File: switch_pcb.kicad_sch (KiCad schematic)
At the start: 6 parts, among them J1 Screw_Terminal_01x04, SW1 SW_Push_SPDT

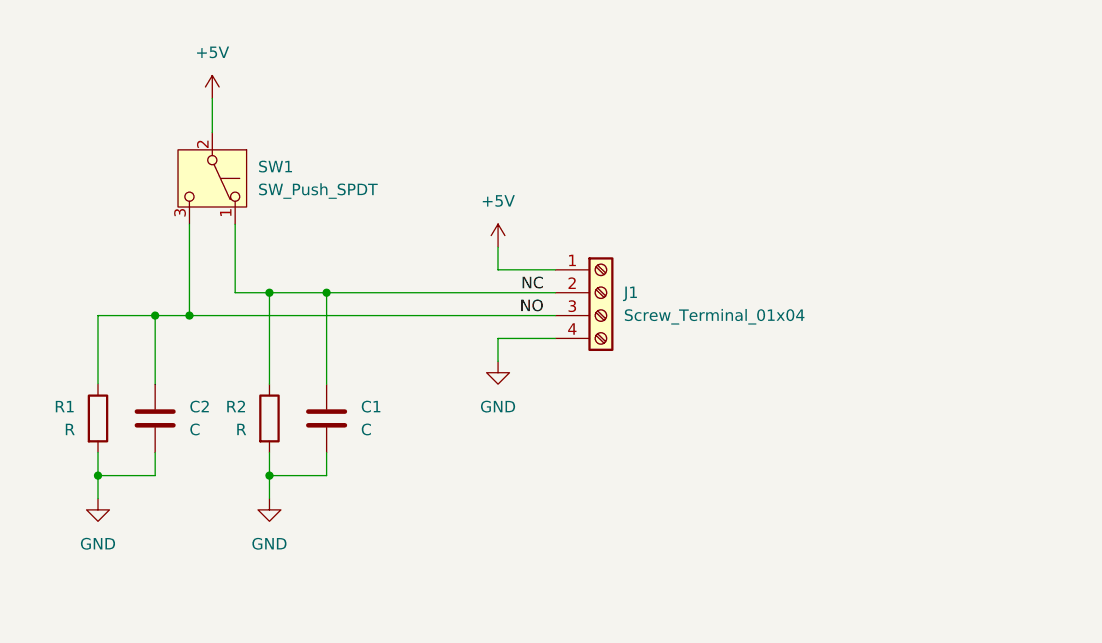
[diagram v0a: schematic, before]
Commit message: Add some footprints and mounting holes
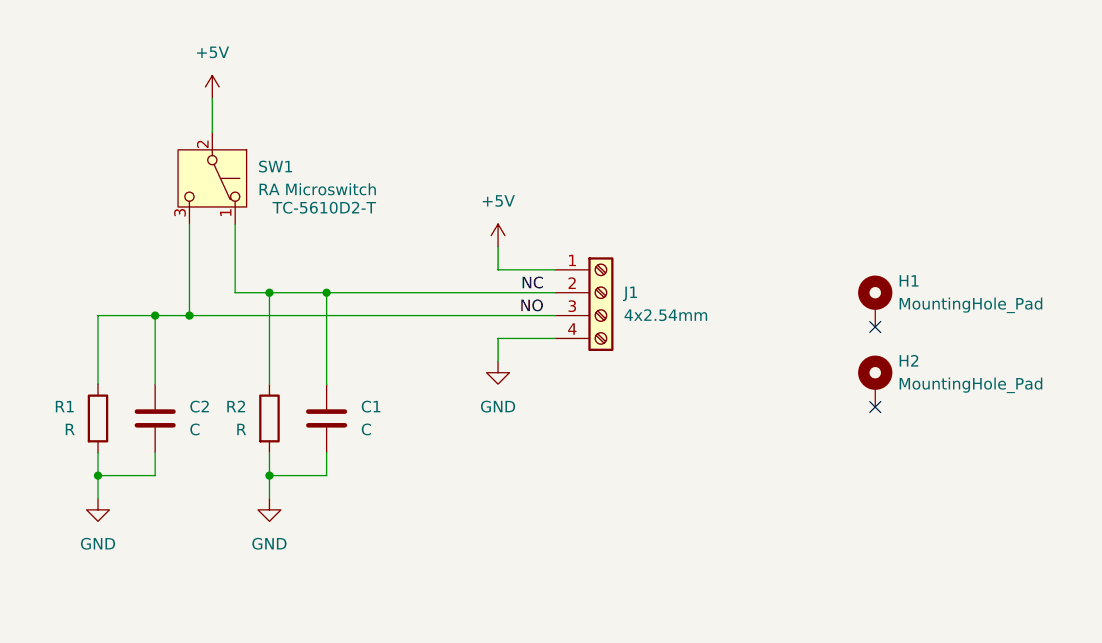
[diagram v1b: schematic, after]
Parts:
- added H1, H2: MountingHole_Pad, symbol Mechanical:MountingHole_Pad
- C1, C2: footprint (none) -> Capacitor_THT:C_Disc_D9.0mm_W5.0mm_P5.00mm
- J1: value Screw_Terminal_01x04 -> 4x2.54mm; footprint (none) -> TerminalBlock_Phoenix:TerminalBlock_Phoenix_MPT-0,5-4-2.54_1x04_P2.54mm_Horizontal; JLC (none) -> C5188444
- R1, R2: footprint (none) -> Resistor_THT:R_Axial_DIN0207_L6.3mm_D2.5mm_P10.16mm_Horizontal
- SW1: value SW_Push_SPDT -> RA Microswitch; JLC (none) -> C504864; MFR (none) -> TC-5610D2-T
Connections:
- no-connect marks 0 -> 2
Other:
- title: (none) -> 2020 Extrusion Microswitch Mount
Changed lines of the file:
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@@
 	(generator_version "8.0")
 	(paper "A4")
+	(title_block
+		(title "2020 Extrusion Microswitch Mount")
+		(comment 1 "All components are through-hole")
+	)
 	(junction
 		(at 127 81.28)
@@
 		(diameter 0)
 		(color 0 0 0 0)
+	)
+	(no_connect
+		(at 187.96 85.09)
+	)
+	(no_connect
+		(at 187.96 93.98)
 	)
 	(wire
@@
 			)
 		)
-		(property "Footprint" ""
+		(property "Footprint" "Resistor_THT:R_Axial_DIN0207_L6.3mm_D2.5mm_P10.16mm_Horizontal"
 			(at 99.822 95.25 90)
 			(effects
@@
 	)
 	(symbol
+		(lib_id "Mechanical:MountingHole_Pad")
+		(at 187.96 82.55 0)
+		(unit 1)
+		(exclude_from_sim yes)
+		(in_bom no)
+		(on_board yes)
+		(dnp no)
+		(fields_autoplaced yes)
+		(property "Reference" "H1"
+			(at 190.5 80.0099 0)
+			(effects
+				(font
+					(size 1.27 1.27)
+				)
+				(justify left)
+			)
+		)
+		(property "Value" "MountingHole_Pad"
+			(at 190.5 82.5499 0)
+			(effects
+				(font
+					(size 1.27 1.27)
+				)
+				(justify left)
+			)
+		)
+		(property "Footprint" ""
+			(at 187.96 82.55 0)
+			(effects
+				(font
+					(size 1.27 1.27)
+				)
+				(hide yes)
+			)
+		)
+		(property "Datasheet" "~"
+			(at 187.96 82.55 0)
+			(effects
+				(font
+					(size 1.27 1.27)
+				)
+				(hide yes)
+			)
+		)
+		(property "Description" "Mounting Hole with connection"
+			(at 187.96 82.55 0)
+			(effects
+				(font
+					(size 1.27 1.27)
+				)
+				(hide yes)
+			)
+		)
+		(pin "1"
+		)
+		(instances
+			(project "switch_pcb"
+				(path "/e6686c7b-f499-4426-8460-934710b4709c"
+					(reference "H1")
+					(unit 1)
+				)
+			)
+		)
+	)
+	(symbol
+		(lib_id "Mechanical:MountingHole_Pad")
+		(at 187.96 91.44 0)
+		(unit 1)
+		(exclude_from_sim yes)
+		(in_bom no)
+		(on_board yes)
+		(dnp no)
+		(fields_autoplaced yes)
+		(property "Reference" "H2"
+			(at 190.5 88.8999 0)
+			(effects
+				(font
+					(size 1.27 1.27)
+				)
+				(justify left)
+			)
+		)
+		(property "Value" "MountingHole_Pad"
+			(at 190.5 91.4399 0)
+			(effects
+				(font
+					(size 1.27 1.27)
+				)
+				(justify left)
+			)
+		)
+		(property "Footprint" ""
+			(at 187.96 91.44 0)
+			(effects
+				(font
+					(size 1.27 1.27)
+				)
+				(hide yes)
+			)
+		)
+		(property "Datasheet" "~"
+			(at 187.96 91.44 0)
+			(effects
+				(font
+					(size 1.27 1.27)
+				)
+				(hide yes)
+			)
+		)
+		(property "Description" "Mounting Hole with connection"
+			(at 187.96 91.44 0)
+			(effects
+				(font
+					(size 1.27 1.27)
+				)
+				(hide yes)
+			)
+		)
+		(pin "1"
+		)
+		(instances
+			(project "switch_pcb"
+				(path "/e6686c7b-f499-4426-8460-934710b4709c"
+					(reference "H2")
+					(unit 1)
+				)
+			)
+		)
+	)
+	(symbol
 		(lib_id "power:GND")
 		(at 120.65 104.14 0)
@@
 			)
 		)
-		(property "Value" "Screw_Terminal_01x04"
+		(property "Value" "4x2.54mm"
 			(at 160.02 83.8199 0)
 			(effects
@@
 			)
 		)
-		(property "Footprint" ""
+		(property "Footprint" "TerminalBlock_Phoenix:TerminalBlock_Phoenix_MPT-0,5-4-2.54_1x04_P2.54mm_Horizontal"
 			(at 157.48 81.28 0)
 			(effects
@@
 			)
 		)
-		(property "Datasheet" "~"
+		(property "Datasheet" "https://www.lcsc.com/datasheet/lcsc_datasheet_2309150913_MAX-MX128-2-54-04P-GN01-Cu-Y-A_C5188444.pdf"
 			(at 157.48 81.28 0)
 			(effects
@@
 		)
 		(property "Description" "Generic screw terminal, single row, 01x04, script generated (kicad-library-utils/schlib/autogen/connector/)"
+			(at 157.48 81.28 0)
+			(effects
+				(font
+					(size 1.27 1.27)
+				)
+				(hide yes)
+			)
+		)
+		(property "JLC" "C5188444"
 			(at 157.48 81.28 0)
 			(effects
@@
 		(on_board yes)
 		(dnp no)
-		(fields_autoplaced yes)
 		(property "Reference" "SW1"
 			(at 119.38 67.3099 90)
@@
 			)
 		)
-		(property "Value" "SW_Push_SPDT"
+		(property "Value" "RA Microswitch"
 			(at 119.38 69.8499 90)
 			(effects
@@
 			)
 		)
-		(property "Datasheet" "~"
+		(property "Datasheet" "https://www.lcsc.com/datasheet/lcsc_datasheet_2004101009_Yuandi-TC-5610D2-T_C504864.pdf"
 			(at 114.3 68.58 0)
 			(effects
@@
 				)
 				(hide yes)
+			)
+		)
+		(property "JLC" "C504864"
+			(at 114.3 68.58 90)
+			(effects
+				(font
+					(size 1.27 1.27)
+				)
+				(hide yes)
+			)
+		)
+		(property "MFR" "TC-5610D2-T "
+			(at 126.746 71.882 90)
+			(effects
+				(font
+					(size 1.27 1.27)
+				)
 			)
 		)
@@
 			)
 		)
-		(property "Footprint" ""
+		(property "Footprint" "Capacitor_THT:C_Disc_D9.0mm_W5.0mm_P5.00mm"
 			(at 108.9152 99.06 0)
 			(effects
@@
 			)
 		)
-		(property "Footprint" ""
+		(property "Footprint" "Resistor_THT:R_Axial_DIN0207_L6.3mm_D2.5mm_P10.16mm_Horizontal"
 			(at 118.872 95.25 90)
 			(effects
@@
 			)
 		)
-		(property "Footprint" ""
+		(property "Footprint" "Capacitor_THT:C_Disc_D9.0mm_W5.0mm_P5.00mm"
 			(at 127.9652 99.06 0)
 			(effects

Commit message: Switch to only breaking out the normally open circuit
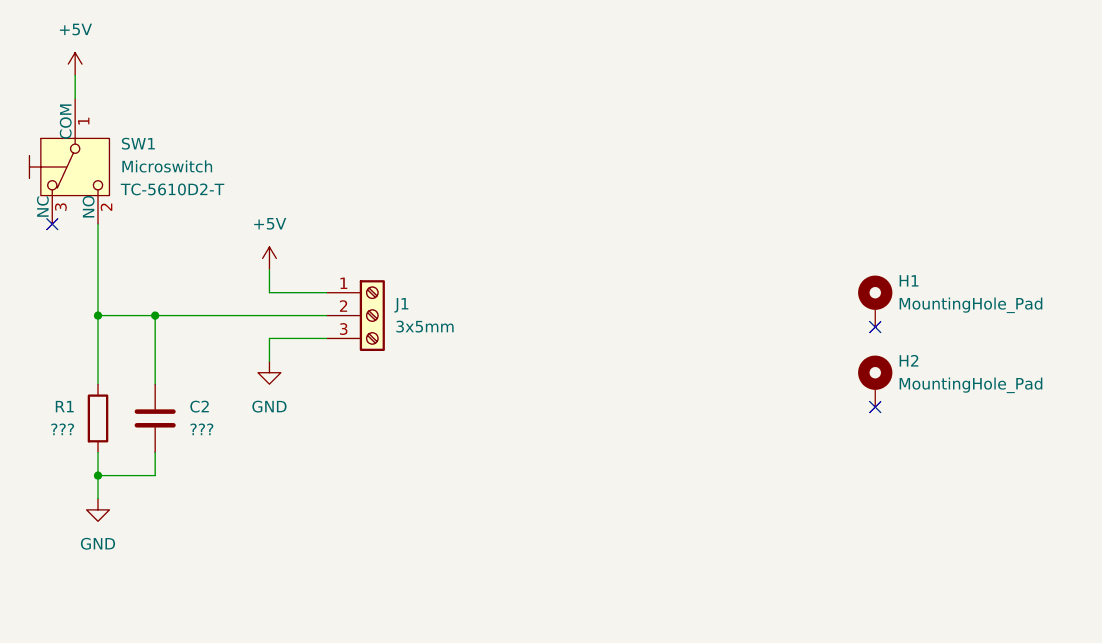
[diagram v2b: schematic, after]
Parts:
- removed C1: C, Capacitor_THT:C_Disc_D9.0mm_W5.0mm_P5.00mm, symbol Device:C
- removed R2: R, Resistor_THT:R_Axial_DIN0207_L6.3mm_D2.5mm_P10.16mm_Horizontal, symbol Device:R
- C2: value C -> ???
- J1: value 4x2.54mm -> 3x5mm; footprint TerminalBlock_Phoenix:TerminalBlock_Phoenix_MPT-0,5-4-2.54_1x04_P2.54mm_Horizontal -> TerminalBlock_Phoenix:TerminalBlock_Phoenix_MKDS-1,5-3_1x03_P5.00mm_Horizontal; symbol Connector:Screw_Terminal_01x04 -> Connector:Screw_Terminal_01x03; JLC C5188444 -> C5188435
- R1: value R -> ???
- SW1: value RA Microswitch -> Microswitch; symbol Switch:SW_Push_SPDT -> microswitch:SW_Push_SPDT
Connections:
- net +5V: now also SW1.1 (COM); no longer SW1.2 (B)
- net GND: now also J1.3 (Pin_3); no longer J1.4 (Pin_4)
- net NC: no longer names the net of J1.2 (Pin_2)
- net NC: now also C2.1, R1.1, SW1.2 (NO); no longer SW1.1 (A)
- removed net NO: C2.1, J1.3 (Pin_3), R1.1, SW1.3 (C)
- no-connect marks 2 -> 3

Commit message: Create footprints
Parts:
- H1, H2: footprint (none) -> MountingHole:MountingHole_5.3mm_M5_ISO7380_Pad
- SW1: footprint (none) -> switch_pcb:TC-5610D2-T
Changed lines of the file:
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@@
 			)
 		)
-		(property "Footprint" ""
+		(property "Footprint" "MountingHole:MountingHole_5.3mm_M5_ISO7380_Pad"
 			(at 187.96 82.55 0)
 			(effects
@@
 			)
 		)
-		(property "Footprint" ""
+		(property "Footprint" "MountingHole:MountingHole_5.3mm_M5_ISO7380_Pad"
 			(at 187.96 91.44 0)
 			(effects
@@
 			)
 		)
-		(property "Footprint" ""
+		(property "Footprint" "switch_pcb:TC-5610D2-T"
 			(at 99.06 67.31 0)
 			(effects

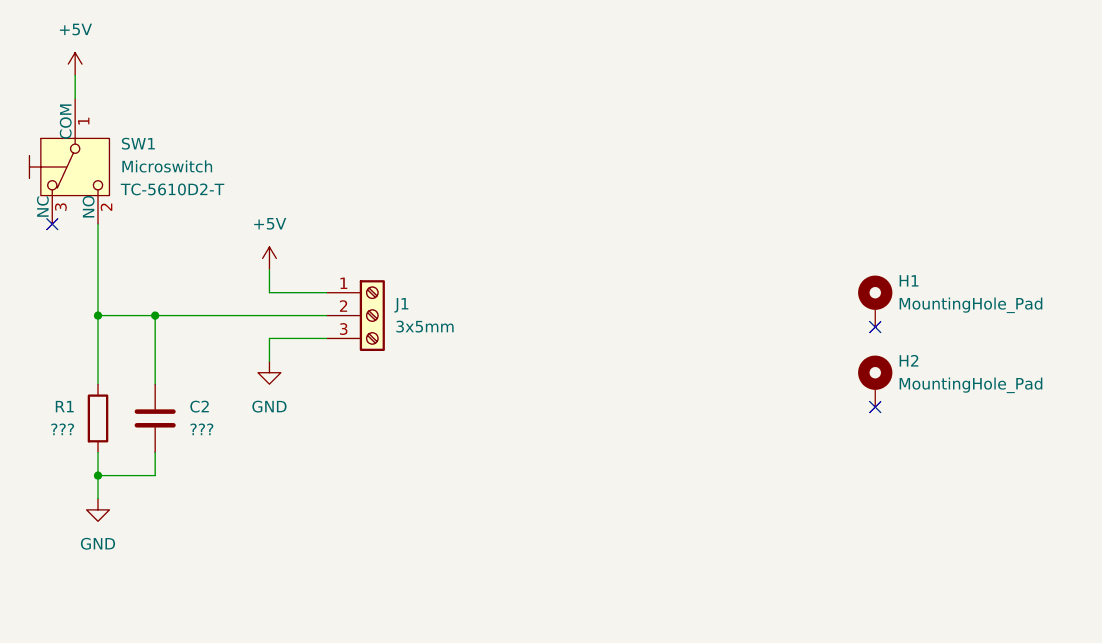
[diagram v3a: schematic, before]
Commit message: Review feedback Center PCB on page Remove 5V plane & use teardrops Change circuit to be pulled up & switched low
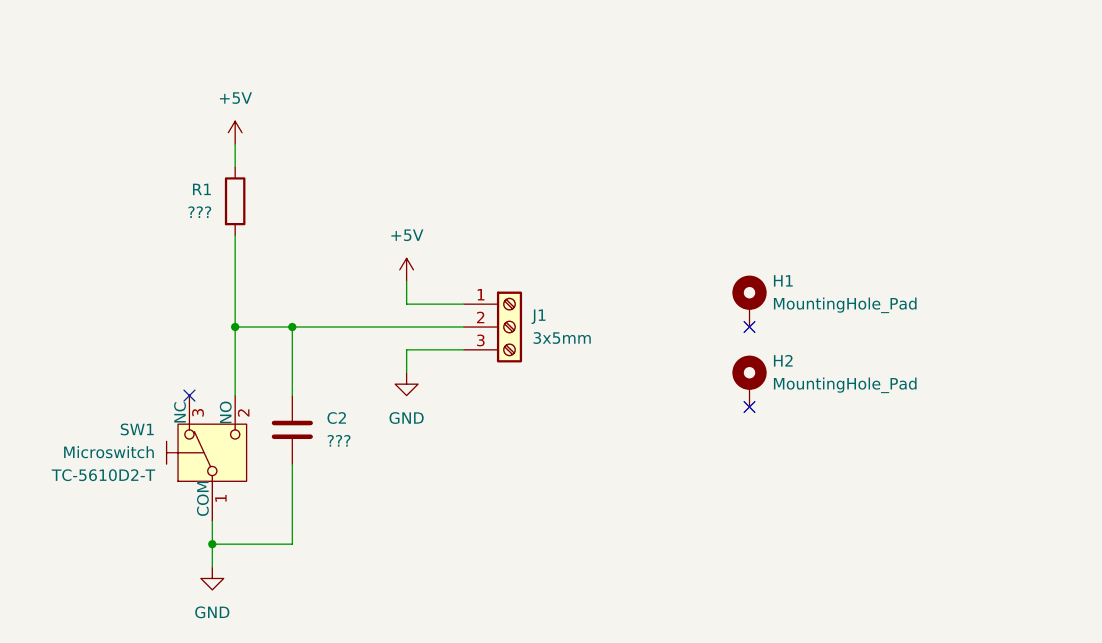
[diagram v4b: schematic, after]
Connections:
- net +5V: now also R1.1; no longer SW1.1 (COM)
- net GND: now also SW1.1 (COM); no longer R1.2
- net at C2.1, J1.2 (Pin_2), SW1.2 (NO): now also R1.2; no longer R1.1
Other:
- moved on the sheet: C2, H1, H2, J1, R1, SW1

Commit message: Switch back to the previous circuit with switch at the top
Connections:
- net +5V: now also SW1.1 (COM); no longer R1.1
- net GND: now also R1.1; no longer SW1.1 (COM)
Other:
- moved on the sheet: C2, R1, SW1
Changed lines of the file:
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@@
 	)
 	(junction
-		(at 114.3 109.22)
+		(at 116.84 102.87)
 		(diameter 0)
 		(color 0 0 0 0)
@@
 	)
 	(no_connect
-		(at 111.76 92.71)
+		(at 111.76 74.93)
 	)
 	(no_connect
@@
 	(wire
 		(pts
-			(xy 114.3 106.68) (xy 114.3 109.22)
+			(xy 116.84 99.06) (xy 116.84 102.87)
 		)
 		(stroke
@@
 	(wire
 		(pts
-			(xy 123.19 85.09) (xy 123.19 92.71)
+			(xy 123.19 85.09) (xy 123.19 91.44)
 		)
 		(stroke
@@
 	(wire
 		(pts
-			(xy 123.19 100.33) (xy 123.19 109.22)
-		)
-		(stroke
-			(width 0)
-			(type default)
-		)
-	)
-	(wire
-		(pts
-			(xy 114.3 109.22) (xy 114.3 111.76)
-		)
-		(stroke
-			(width 0)
-			(type default)
-		)
-	)
-	(wire
-		(pts
-			(xy 116.84 64.77) (xy 116.84 67.31)
+			(xy 123.19 99.06) (xy 123.19 102.87)
+		)
+		(stroke
+			(width 0)
+			(type default)
+		)
+	)
+	(wire
+		(pts
+			(xy 116.84 102.87) (xy 116.84 105.41)
+		)
+		(stroke
+			(width 0)
+			(type default)
+		)
+	)
+	(wire
+		(pts
+			(xy 114.3 58.42) (xy 114.3 60.96)
 		)
 		(stroke
@@
 	(wire
 		(pts
-			(xy 116.84 92.71) (xy 116.84 85.09)
-		)
-		(stroke
-			(width 0)
-			(type default)
-		)
-	)
-	(wire
-		(pts
-			(xy 114.3 109.22) (xy 123.19 109.22)
+			(xy 116.84 91.44) (xy 116.84 85.09)
+		)
+		(stroke
+			(width 0)
+			(type default)
+		)
+	)
+	(wire
+		(pts
+			(xy 116.84 102.87) (xy 123.19 102.87)
 		)
 		(stroke
@@
 	(symbol
 		(lib_id "power:GND")
-		(at 114.3 111.76 0)
+		(at 116.84 105.41 0)
 		(unit 1)
 		(exclude_from_sim no)
@@
 		(fields_autoplaced yes)
 		(property "Reference" "#PWR06"
-			(at 114.3 118.11 0)
+			(at 116.84 111.76 0)
 			(effects
 				(font
@@
 		)
 		(property "Value" "GND"
-			(at 114.3 116.84 0)
+			(at 116.84 110.49 0)
 			(effects
 				(font
@@
 		)
 		(property "Footprint" ""
-			(at 114.3 111.76 0)
+			(at 116.84 105.41 0)
 			(effects
 				(font
@@
 		)
 		(property "Datasheet" ""
-			(at 114.3 111.76 0)
+			(at 116.84 105.41 0)
 			(effects
 				(font
@@
 		)
 		(property "Description" "Power symbol creates a global label with name \"GND\" , ground"
-			(at 114.3 111.76 0)
+			(at 116.84 105.41 0)
 			(effects
 				(font
@@
 	(symbol
 		(lib_id "Device:R")
-		(at 116.84 71.12 0)
+		(at 116.84 95.25 180)
 		(unit 1)
 		(exclude_from_sim no)
@@
 		(fields_autoplaced yes)
 		(property "Reference" "R1"
-			(at 114.3 69.8499 0)
-			(effects
-				(font
-					(size 1.27 1.27)
-				)
-				(justify right)
+			(at 114.3 93.9799 0)
+			(effects
+				(font
+					(size 1.27 1.27)
+				)
+				(justify left)
 			)
 		)
 		(property "Value" "???"
-			(at 114.3 72.3899 0)
-			(effects
-				(font
-					(size 1.27 1.27)
-				)
-				(justify right)
+			(at 114.3 96.5199 0)
+			(effects
+				(font
+					(size 1.27 1.27)
+				)
+				(justify left)
 			)
 		)
 		(property "Footprint" "Resistor_THT:R_Axial_DIN0207_L6.3mm_D2.5mm_P10.16mm_Horizontal"
-			(at 115.062 71.12 90)
+			(at 118.618 95.25 90)
 			(effects
 				(font
@@
 		)
 		(property "Datasheet" "~"
-			(at 116.84 71.12 0)
+			(at 116.84 95.25 0)
 			(effects
 				(font
@@
 		)
 		(property "Description" "Resistor"
-			(at 116.84 71.12 0)
+			(at 116.84 95.25 0)
 			(effects
 				(font
@@
 	(symbol
 		(lib_id "power:+5V")
-		(at 116.84 64.77 0)
+		(at 114.3 58.42 0)
 		(unit 1)
 		(exclude_from_sim no)
@@
 		(fields_autoplaced yes)
 		(property "Reference" "#PWR03"
-			(at 116.84 68.58 0)
+			(at 114.3 62.23 0)
 			(effects
 				(font
@@
 		)
 		(property "Value" "+5V"
-			(at 116.84 59.69 0)
+			(at 114.3 53.34 0)
 			(effects
 				(font
@@
 		)
 		(property "Footprint" ""
-			(at 116.84 64.77 0)
+			(at 114.3 58.42 0)
 			(effects
 				(font
@@
 		)
 		(property "Datasheet" ""
-			(at 116.84 64.77 0)
+			(at 114.3 58.42 0)
 			(effects
 				(font
@@
 		)
 		(property "Description" "Power symbol creates a global label with name \"+5V\""
-			(at 116.84 64.77 0)
+			(at 114.3 58.42 0)
 			(effects
 				(font
@@
 	(symbol
 		(lib_id "microswitch:SW_Push_SPDT")
-		(at 114.3 99.06 90)
+		(at 114.3 68.58 90)
+		(mirror x)
 		(unit 1)
 		(exclude_from_sim no)
@@
 		(dnp no)
 		(property "Reference" "SW1"
-			(at 107.95 96.5199 90)
+			(at 107.95 71.1201 90)
 			(effects
 				(font
@@
 		)
 		(property "Value" "Microswitch"
-			(at 107.95 99.0599 90)
+			(at 107.95 68.5801 90)
 			(effects
 				(font
@@
 		)
 		(property "Footprint" "switch_pcb:TC-5610D2-T"
-			(at 114.3 99.06 0)
+			(at 114.3 68.58 0)
 			(effects
 				(font
@@
 		)
 		(property "Datasheet" "https://www.lcsc.com/datasheet/lcsc_datasheet_2004101009_Yuandi-TC-5610D2-T_C504864.pdf"
-			(at 114.3 99.06 0)
+			(at 114.3 68.58 0)
 			(effects
 				(font
@@
 		)
 		(property "Description" "Momentary Switch, single pole double throw"
-			(at 105.41 99.06 0)
+			(at 105.41 68.58 0)
 			(effects
 				(font
@@
 		)
 		(property "JLC" "C504864"
-			(at 114.3 99.06 90)
+			(at 114.3 68.58 90)
 			(effects
 				(font
@@
 		)
 		(property "MFR" "TC-5610D2-T "
-			(at 107.95 101.5999 90)
+			(at 107.95 66.0401 90)
 			(effects
 				(font
@@
 	(symbol
 		(lib_id "Device:C")
-		(at 123.19 96.52 0)
+		(at 123.19 95.25 0)
 		(unit 1)
 		(exclude_from_sim no)
@@
 		(fields_autoplaced yes)
 		(property "Reference" "C2"
-			(at 127 95.2499 0)
+			(at 127 93.9799 0)
 			(effects
 				(font
@@
 		)
 		(property "Value" "???"
-			(at 127 97.7899 0)
+			(at 127 96.5199 0)
 			(effects
 				(font
@@
 		)
 		(property "Footprint" "Capacitor_THT:C_Disc_D9.0mm_W5.0mm_P5.00mm"
-			(at 124.1552 100.33 0)
+			(at 124.1552 99.06 0)
 			(effects
 				(font
@@
 		)
 		(property "Datasheet" "~"
-			(at 123.19 96.52 0)
+			(at 123.19 95.25 0)
 			(effects
 				(font
@@
 		)
 		(property "Description" "Unpolarized capacitor"
-			(at 123.19 96.52 0)
-			(effects
-				(font
+			(at 123.19 95.25 0)
+			(effects
+				(font

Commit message: Update to "UoS Robotics Summer School" Switch to UoS logo Update to Kicad v9
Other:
- title: 2020 Extrusion Microswitch Mount -> 2026 Extrusion Microswitch Mount
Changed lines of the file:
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@@
 (kicad_sch
-	(version 20231120)
+	(version 20250114)
 	(generator "eeschema")
-	(generator_version "8.0")
+	(generator_version "9.0")
 	(paper "A4")
 	(title_block
-		(title "2020 Extrusion Microswitch Mount")
+		(title "2026 Extrusion Microswitch Mount")
+		(rev "1.1")
 		(comment 1 "All components are through-hole")
 	)
@@
 		)
 	)
+	(embedded_fonts no)
 )
